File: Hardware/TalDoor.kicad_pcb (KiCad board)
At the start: 2 copper layers, 48 parts, among them J1 SI-52003-F_RJ45, P1 Conn_02x18_Odd_Even, P2 Conn_02x18_Odd_Even, U1 DRV8837, U2 ENC28J60-C/SS, U3 PN532, U4 AG9700, Y1 25MHz

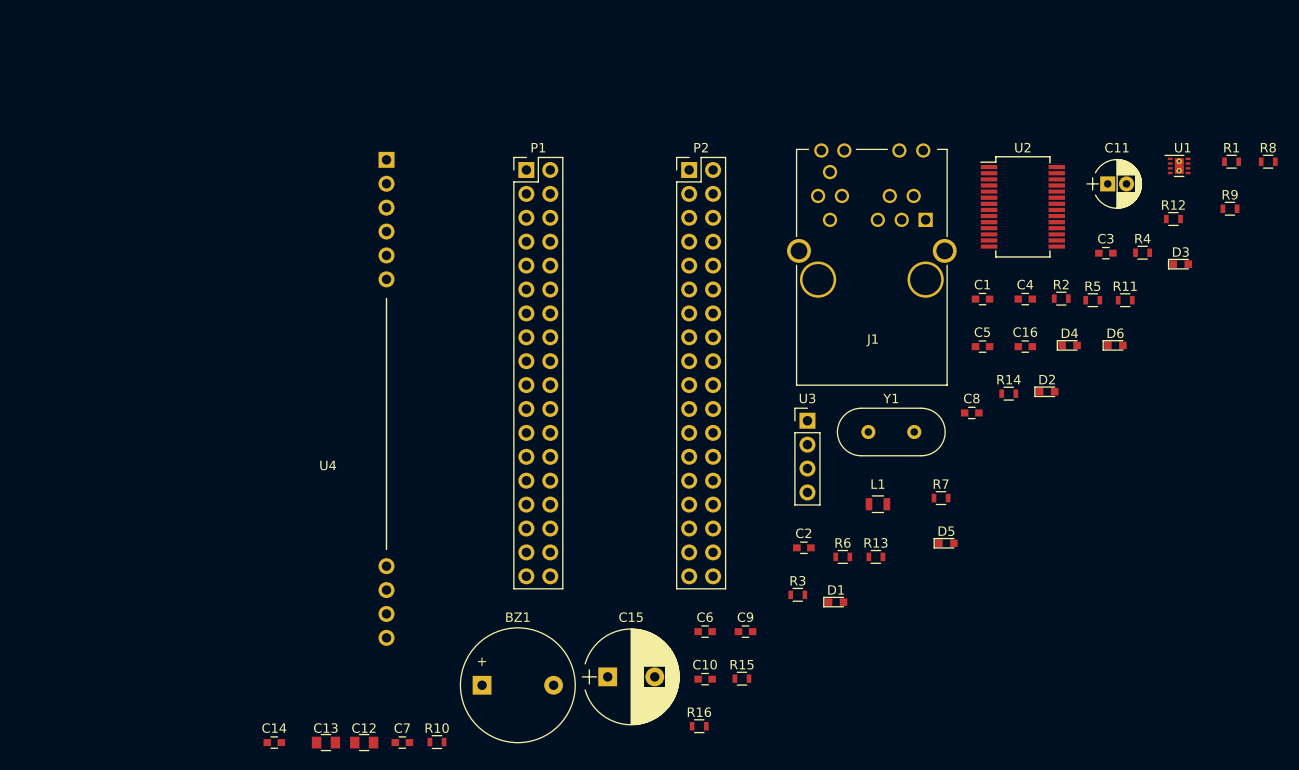
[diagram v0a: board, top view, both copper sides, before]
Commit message: Added connectors, moved notifications to external PCB
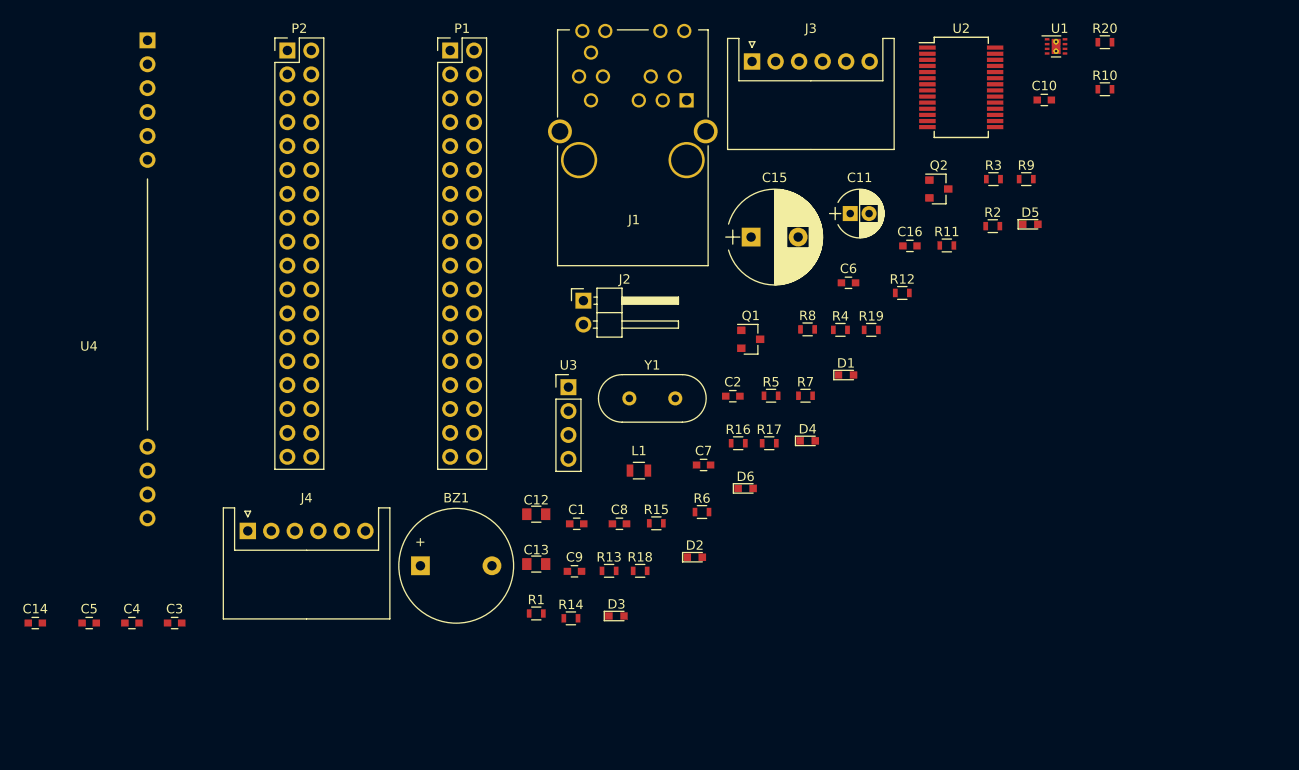
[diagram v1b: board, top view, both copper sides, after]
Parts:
- added J2: Screw_Terminal_01x02, Pin_Headers:Pin_Header_Angled_1x02_Pitch2.54mm, F.Cu at (200.1, 74.3)
- added J3: Conn_01x06_Male, Connectors_JST:JST_XH_S06B-XH-A_06x2.50mm_Angled, F.Cu at (218.1, 48.9)
- added J4: Conn_01x06_Male, Connectors_JST:JST_XH_S06B-XH-A_06x2.50mm_Angled, F.Cu at (164.5, 98.8)
- added Q1: RK7002BM, TO_SOT_Packages_SMD:SOT-23, F.Cu at (217.9, 78.4)
- added Q2: RK7002BM, TO_SOT_Packages_SMD:SOT-23, F.Cu at (237.9, 62.5)
- added R17: 180, Resistors_SMD:R_0603, F.Cu at (219.9, 89.5)
- added R18: 10k, Resistors_SMD:R_0603, F.Cu at (206.2, 103.1)
- added R19: 180, Resistors_SMD:R_0603, F.Cu at (230.7, 77.4)
- added R20: 10k, Resistors_SMD:R_0603, F.Cu at (255.6, 46.9)
- moved C3 106.5 mm to (156.7, 108.6)
- moved C4 101.0 mm to (152.2, 108.6)
- moved C5 99.4 mm to (147.6, 108.6)
- moved R10 99.3 mm to (255.6, 51.9)
- moved R1 88.1 mm to (195.1, 107.6)
- moved C10 71.3 mm to (249.1, 53.0)
- moved D3 70.7 mm to (203.7, 107.9)
- moved R14 52.3 mm to (198.8, 108.1)
- moved R8 52.1 mm to (224.0, 77.4)
- moved C1 49.3 mm to (199.4, 98.1)
- moved C15 49.2 mm to (218.0, 67.6)
- moved R3 48.8 mm to (243.7, 61.4)
- moved P2 44.5 mm to (168.7, 47.8)
- moved C7 43.5 mm to (212.9, 91.8)
- moved D6 42.1 mm to (217.4, 94.3)
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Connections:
- D1 pad 1: GND -> Net-(D1-Pad1)
- D1 pad 2: Net-(D1-Pad2) -> +3V3
- D2 pad 1: GND -> Net-(D2-Pad1)
- D2 pad 2: Net-(D2-Pad2) -> +3V3
- D3 pad 1: GND -> Net-(D3-Pad1)
- D3 pad 2: Net-(D3-Pad2) -> +3V3
- D4 pad 1: GND -> Net-(D4-Pad1)
- D4 pad 2: Net-(D4-Pad2) -> +3V3
- D5 pad 1: GND -> Net-(D5-Pad1)
- D5 pad 2: Net-(D5-Pad2) -> +3V3
- D6 pad 1: GND -> Net-(D6-Pad1)
- D6 pad 2: Net-(D6-Pad2) -> +3V3
- P2 pad 28: /PRU0_6 -> Net-(P2-Pad28)
- P2 pad 30: /PRU0_3 -> Net-(P2-Pad30)
- P2 pad 32: /PRU0_2 -> Net-(P2-Pad32)
- P2 pad 34: /PRU0_5 -> Net-(P2-Pad34)
- R10 pad 1: /PRU0_3 -> Net-(D1-Pad1)
- R10 pad 2: Net-(D1-Pad2) -> Net-(Q1-Pad3)
- R11 pad 1: /PRU0_2 -> Net-(D2-Pad1)
- R11 pad 2: Net-(D2-Pad2) -> Net-(Q1-Pad3)
- R12 pad 1: /PRU0_5 -> Net-(D3-Pad1)
- R12 pad 2: Net-(D3-Pad2) -> Net-(Q1-Pad3)
- R13 pad 1: /PRU0_0 -> Net-(D4-Pad1)
- R13 pad 2: Net-(D4-Pad2) -> Net-(Q2-Pad3)
- R14 pad 1: /PRU0_4 -> Net-(D5-Pad1)
- R14 pad 2: Net-(D5-Pad2) -> Net-(Q2-Pad3)
- R15 pad 1: /PRU0_7 -> Net-(D6-Pad1)
- R15 pad 2: Net-(D6-Pad2) -> Net-(Q2-Pad3)
- U1 pad 6: /PRU0_6 -> /PRU0_4
- U3 pad 1: GND -> Net-(J4-Pad2)
- U3 pad 2: +3V3 -> Net-(J4-Pad1)
- U3 pad 3: /SDA -> Net-(J4-Pad5)
- U3 pad 4: /SCL -> Net-(J4-Pad6)

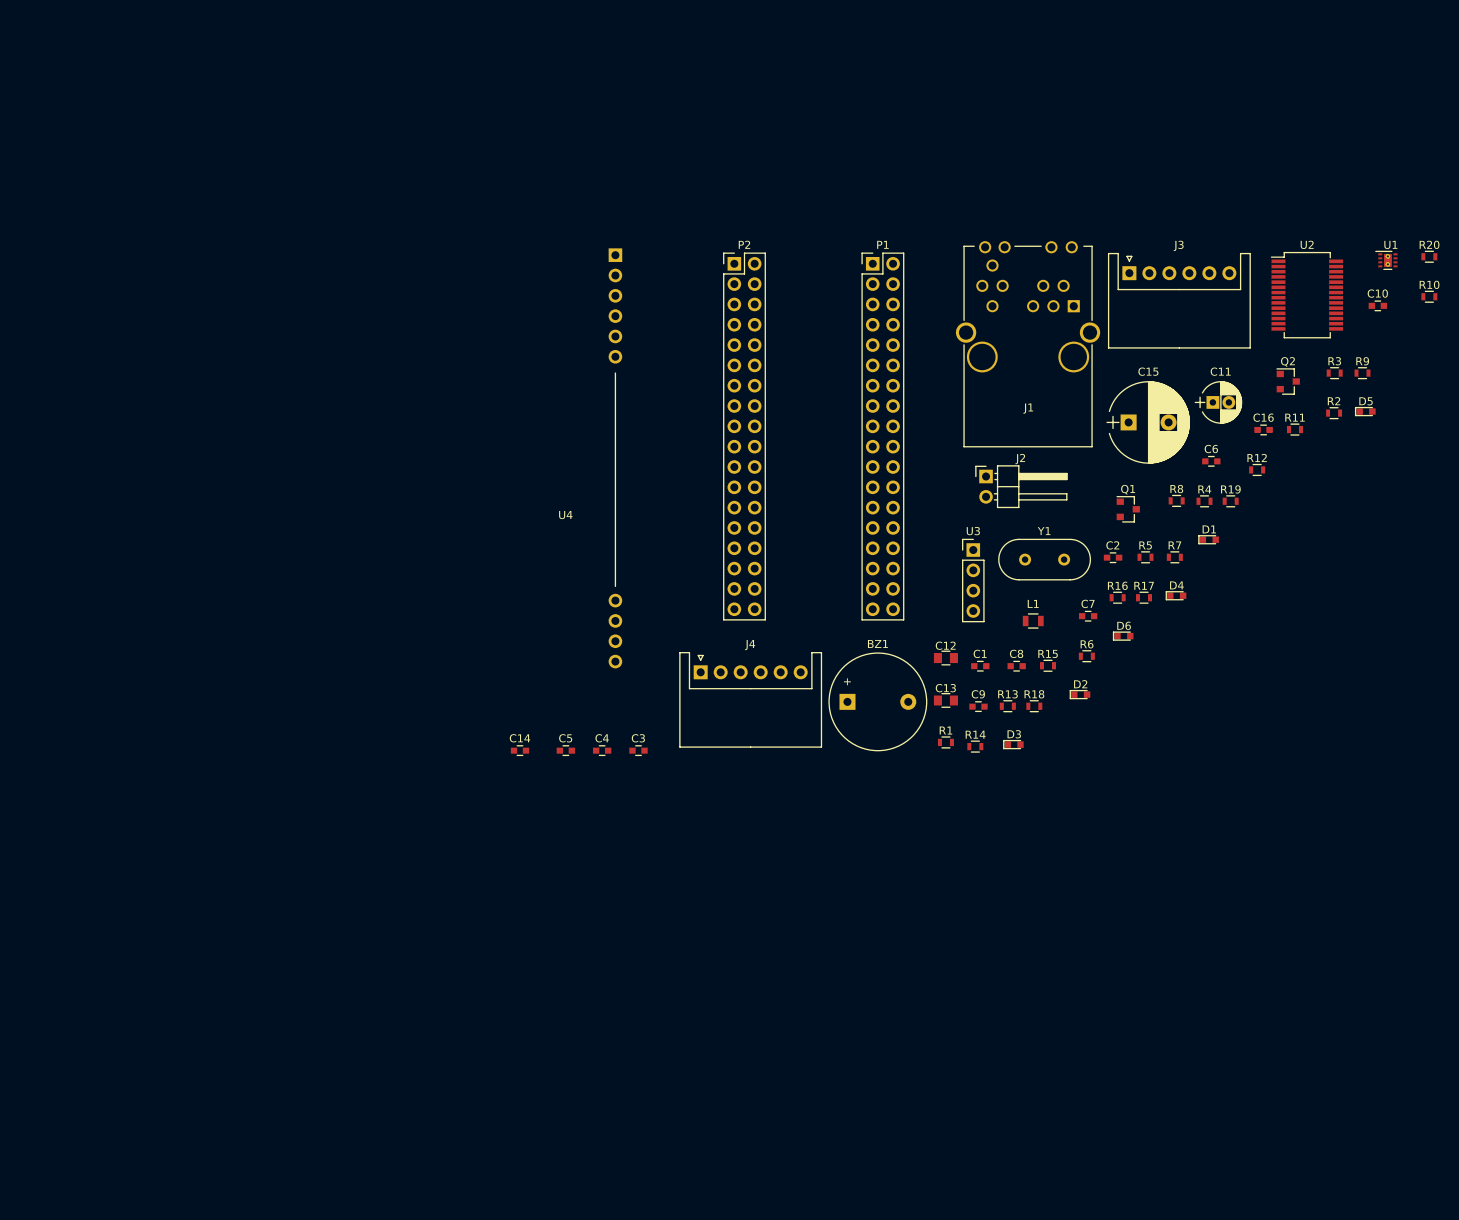
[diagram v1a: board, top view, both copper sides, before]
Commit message: Solution to 1 wire LED nitification issue. See LED_NotificationModel.txt
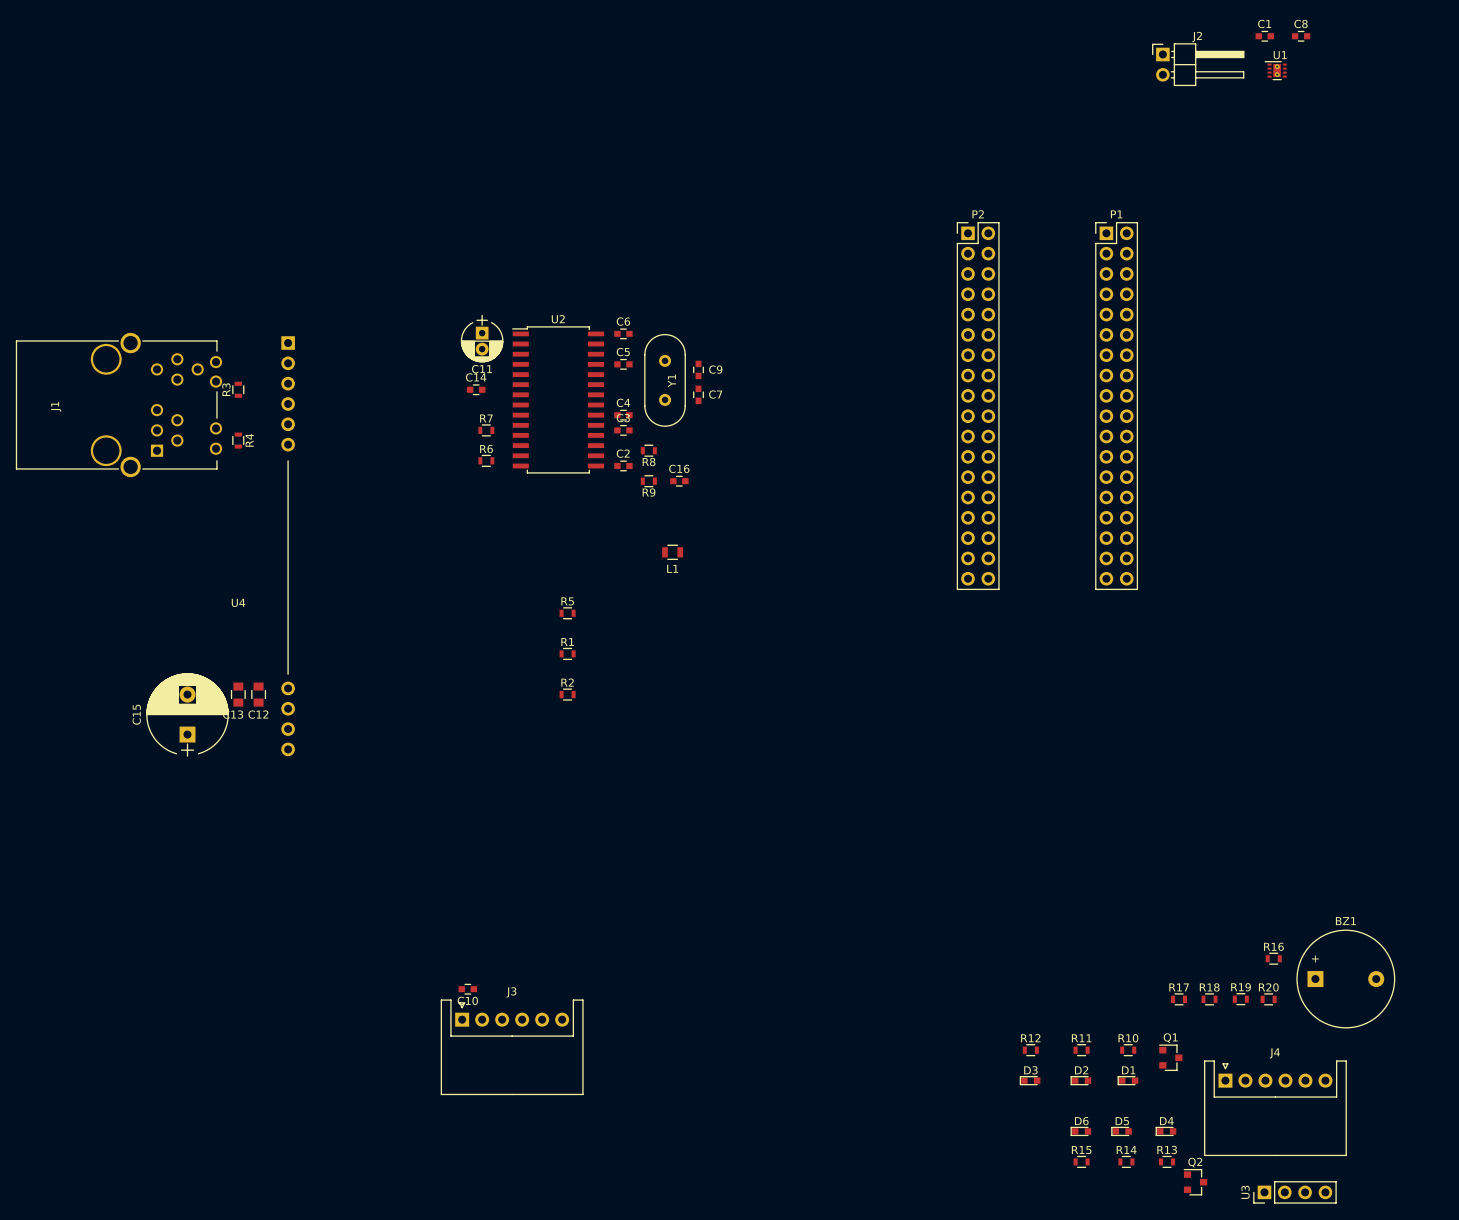
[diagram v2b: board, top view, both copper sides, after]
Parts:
- U2: value ENC28J60-C/SS -> ENC28J60-I/SO; footprint Housings_SSOP:SSOP-28_5.3x10.2mm_Pitch0.65mm -> Housings_SOIC:SOIC-28W_7.5x17.9mm_Pitch1.27mm
- moved C10 142.3 mm to (135.4, 138.4), turned to 180 degrees
- moved R3 137.1 mm to (106.7, 63.5), turned to 90 degrees
- moved J3 125.2 mm to (134.7, 142.2)
- moved C15 123.9 mm to (100.3, 106.6), turned to 90 degrees
- moved R4 121.0 mm to (106.7, 69.8), turned to 270 degrees
- moved J1 109.5 mm to (90.2, 59.7), turned to 270 degrees
- moved R2 102.1 mm to (147.8, 101.6)
- moved R10 101.4 mm to (217.9, 146.1)
- moved Q2 100.8 mm to (226.3, 162.6)
- moved D5 95.0 mm to (217.2, 156.2)
- moved R20 95.0 mm to (235.5, 139.7)
- moved U2 94.5 mm to (146.7, 64.8)
- moved C11 91.8 mm to (137.2, 56.4), turned to 270 degrees
- moved R9 90.2 mm to (158.0, 74.9), turned to 180 degrees
- moved C13 88.5 mm to (106.7, 101.6), turned to 90 degrees
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
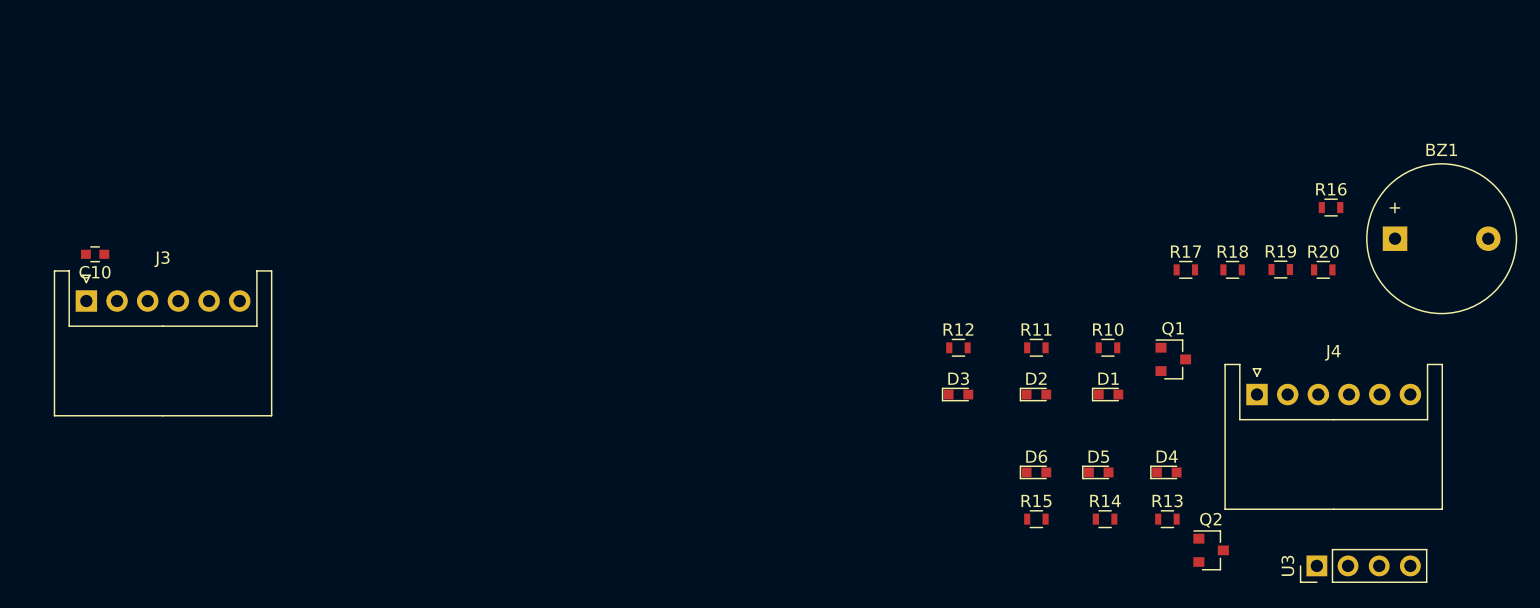
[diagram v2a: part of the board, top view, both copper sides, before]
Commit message: Updated schematic with N/Pmos LED format for single IO drive. Updated BOM
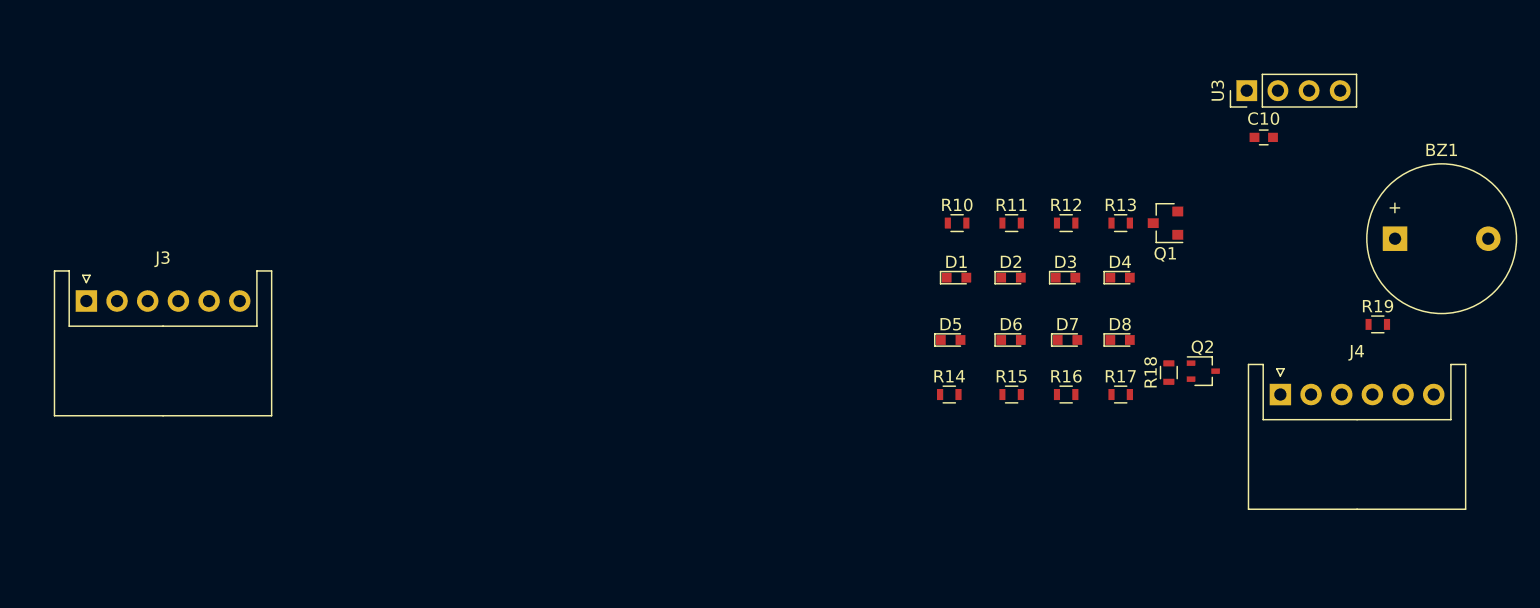
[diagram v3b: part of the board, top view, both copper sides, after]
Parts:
- removed R20: 10k, Resistors_SMD:R_0603
- added D7: R_LED, LEDs:LED_0603, F.Cu at (214.6, 145.4)
- added D8: R_LED, LEDs:LED_0603, F.Cu at (218.9, 145.4)
- D4: value R_LED -> G_LED
- Q2: value RK7002BM -> BSS223PWH6327XTSA1; footprint TO_SOT_Packages_SMD:SOT-23 -> TO_SOT_Packages_SMD:SOT-323_SC-70
- R16: value 150 -> 68
- R17: value 180 -> 68
- R19: value 180 -> 150
- moved C10 95.7 mm to (230.6, 128.9), turned to 0 degrees
- moved U3 39.2 mm to (229.2, 125.1)
- moved R16 26.4 mm to (214.5, 149.9)
- moved R13 24.4 mm to (219.0, 135.9)
- moved D4 16.3 mm to (218.9, 140.3)
- moved R14 16.3 mm to (205.0, 149.9)
- moved D5 16.2 mm to (205.1, 145.4)
- moved R10 15.9 mm to (205.6, 135.9)
- moved D1 15.6 mm to (205.6, 140.3)
- moved Q2 14.6 mm to (225.7, 148.0)
- moved R12 13.4 mm to (214.5, 135.9)
- moved D3 12.9 mm to (214.5, 140.3)
- moved R17 11.5 mm to (219.0, 149.9)
- moved Q1 11.1 mm to (222.6, 135.9), turned to 180 degrees
- moved D6 11.0 mm to (210.0, 145.4)
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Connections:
- C10 pad 1: GND -> Net-(C10-Pad1)
- C10 pad 2: +3V3 -> Net-(C10-Pad2)
- D5 pad 2: +3V3 -> Net-(D5-Pad2)
- D6 pad 2: +3V3 -> Net-(D5-Pad2)
- J3 pad 4: /PRU0_7 -> /PRU1_10
- J4 pad 1: Net-(J4-Pad1) -> Net-(C10-Pad2)
- J4 pad 2: Net-(J4-Pad2) -> Net-(C10-Pad1)
- J4 pad 3: /PRU0_0 -> Net-(J4-Pad3)
- J4 pad 4: /PRU0_7 -> Net-(J4-Pad4)
- P1 pad 29: /PRU0_7 -> Net-(P1-Pad29)
- Q1 pad 1: Net-(Q1-Pad1) -> Net-(J4-Pad3)
- Q2 pad 1: Net-(Q2-Pad1) -> Net-(J4-Pad3)
- Q2 pad 2: GND -> Net-(D5-Pad2)
- Q2 pad 3: Net-(Q2-Pad3) -> +3V3
- R13 pad 2: Net-(Q2-Pad3) -> Net-(Q1-Pad3)
- R14 pad 2: Net-(Q2-Pad3) -> GND
- R15 pad 2: Net-(Q2-Pad3) -> GND
- R16 pad 1: /PRU1_10 -> Net-(D7-Pad1)
- R16 pad 2: Net-(BZ1-Pad1) -> GND
- R17 pad 1: /PRU0_7 -> Net-(D8-Pad1)
- R17 pad 2: Net-(Q1-Pad1) -> GND
- R18 pad 2: Net-(Q1-Pad1) -> Net-(J4-Pad3)
- R19 pad 1: /PRU0_0 -> Net-(J4-Pad4)
- R19 pad 2: Net-(Q2-Pad1) -> Net-(BZ1-Pad1)
- U3 pad 1: Net-(J4-Pad2) -> Net-(C10-Pad1)
- U3 pad 2: Net-(J4-Pad1) -> Net-(C10-Pad2)
